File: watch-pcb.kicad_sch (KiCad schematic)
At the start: 12 parts, among them J1 DAUGHTER

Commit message: quicksaving pcb bc im gonna redo it
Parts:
- removed R1, R2, R8: 10k, Resistor_SMD:R_0402_1005Metric, symbol Device:R
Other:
- removed sheet STM MCU
- added sheet ESP MCU (esp_mcu.kicad_sch)
- sheet IO ports: added ALT_SCL, ALT_SDA, HBT_SCL, HBT_SDA, IMU_SCL, IMU_SDA, MAG_SCL, MAG_SDA, MTR_SCL, MTR_SDA, SD_CLK, SD_CMD, SD_D0, SD_D1, SD_D2, SD_D3, TP_SCL, TP_SDA; removed SCL1, SCL2, SCL3, SDA1, SDA2, SDA3, TP_COM_EN
- sheet USB and Power ports: added USB_DM, USB_DP; removed BOOT, MCU_RST, UART_RX, UART_TX
- moved on the sheet: D1, D15, J1, R3, R4, R5, R55, R6, R7

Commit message: no more daughter probably
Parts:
- renumbered D15 to D1, D1 to D2, R4 to R1, R5 to R2, R6 to R3, R7 to R4, R55 to R5, R3 to R6
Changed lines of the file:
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@@
 		(on_board yes)
 		(dnp no)
-		(property "Reference" "#PWR06"
+		(property "Reference" "#PWR01"
 			(at 224.79 27.94 0)
 			(effects
@@
 			(project "watch-pcb"
 				(path "/b7b86b03-b0df-4b4e-be1d-606605306dad"
-					(reference "#PWR06")
+					(reference "#PWR01")
 					(unit 1)
 				)
@@
 		(on_board yes)
 		(dnp no)
-		(property "Reference" "R6"
+		(property "Reference" "R3"
 			(at 228.6 29.21 0)
 			(effects
@@
 			(project "watch-pcb"
 				(path "/b7b86b03-b0df-4b4e-be1d-606605306dad"
-					(reference "R6")
+					(reference "R3")
 					(unit 1)
 				)
@@
 		(on_board yes)
 		(dnp no)
-		(property "Reference" "#PWR05"
+		(property "Reference" "#PWR03"
 			(at 69.85 118.11 0)
 			(effects
@@
 			(project "watch-pcb"
 				(path "/b7b86b03-b0df-4b4e-be1d-606605306dad"
-					(reference "#PWR05")
+					(reference "#PWR03")
 					(unit 1)
 				)
@@
 		(on_board yes)
 		(dnp no)
-		(property "Reference" "R3"
+		(property "Reference" "R6"
 			(at 69.85 162.56 90)
 			(effects
@@
 			(project "watch-pcb"
 				(path "/b7b86b03-b0df-4b4e-be1d-606605306dad"
-					(reference "R3")
+					(reference "R6")
 					(unit 1)
 				)
@@
 		(on_board yes)
 		(dnp no)
-		(property "Reference" "#PWR03"
+		(property "Reference" "#PWR02"
 			(at 63.5 118.11 0)
 			(effects
@@
 			(project "watch-pcb"
 				(path "/b7b86b03-b0df-4b4e-be1d-606605306dad"
-					(reference "#PWR03")
+					(reference "#PWR02")
 					(unit 1)
 				)
@@
 		(on_board yes)
 		(dnp no)
-		(property "Reference" "D15"
+		(property "Reference" "D1"
 			(at 60.96 154.94 0)
 			(effects
@@
 			(project "watch-pcb"
 				(path "/b7b86b03-b0df-4b4e-be1d-606605306dad"
-					(reference "D15")
+					(reference "D1")
 					(unit 1)
 				)
@@
 		(dnp no)
 		(fields_autoplaced yes)
-		(property "Reference" "#PWR021"
+		(property "Reference" "#PWR05"
 			(at 50.8 160.02 0)
 			(effects
@@
 			(project "watch-pcb"
 				(path "/b7b86b03-b0df-4b4e-be1d-606605306dad"
-					(reference "#PWR021")
+					(reference "#PWR05")
 					(unit 1)
 				)
@@
 		(on_board yes)
 		(dnp no)
-		(property "Reference" "R7"
+		(property "Reference" "R4"
 			(at 237.49 29.21 0)
 			(effects
@@
 			(project "watch-pcb"
 				(path "/b7b86b03-b0df-4b4e-be1d-606605306dad"
-					(reference "R7")
+					(reference "R4")
 					(unit 1)
 				)
@@
 		(dnp no)
 		(fields_autoplaced yes)
-		(property "Reference" "#PWR01"
+		(property "Reference" "#PWR06"
 			(at 50.8 165.1 0)
 			(effects
@@
 			(project "watch-pcb"
 				(path "/b7b86b03-b0df-4b4e-be1d-606605306dad"
-					(reference "#PWR01")
+					(reference "#PWR06")
 					(unit 1)
 				)
@@
 		(on_board yes)
 		(dnp no)
-		(property "Reference" "R4"
+		(property "Reference" "R1"
 			(at 215.9 29.21 0)
 			(effects
@@
 			(project "watch-pcb"
 				(path "/b7b86b03-b0df-4b4e-be1d-606605306dad"
-					(reference "R4")
+					(reference "R1")
 					(unit 1)
 				)
@@
 		(on_board yes)
 		(dnp no)
-		(property "Reference" "R55"
+		(property "Reference" "R5"
 			(at 69.85 157.48 90)
 			(effects
@@
 			(project "watch-pcb"
 				(path "/b7b86b03-b0df-4b4e-be1d-606605306dad"
-					(reference "R55")
+					(reference "R5")
 					(unit 1)
 				)
@@
 		(on_board yes)
 		(dnp no)
-		(property "Reference" "D1"
+		(property "Reference" "D2"
 			(at 62.23 167.64 0)
 			(effects
@@
 			(project "watch-pcb"
 				(path "/b7b86b03-b0df-4b4e-be1d-606605306dad"
-					(reference "D1")
+					(reference "D2")
 					(unit 1)
 				)
@@
 		(on_board yes)
 		(dnp no)
-		(property "Reference" "R5"
+		(property "Reference" "R2"
 			(at 224.79 29.21 0)
 			(effects
@@
 			(project "watch-pcb"
 				(path "/b7b86b03-b0df-4b4e-be1d-606605306dad"
-					(reference "R5")
-					(unit 1)
-				)
+					(reference "R2")
+					(unit 1)
+				)

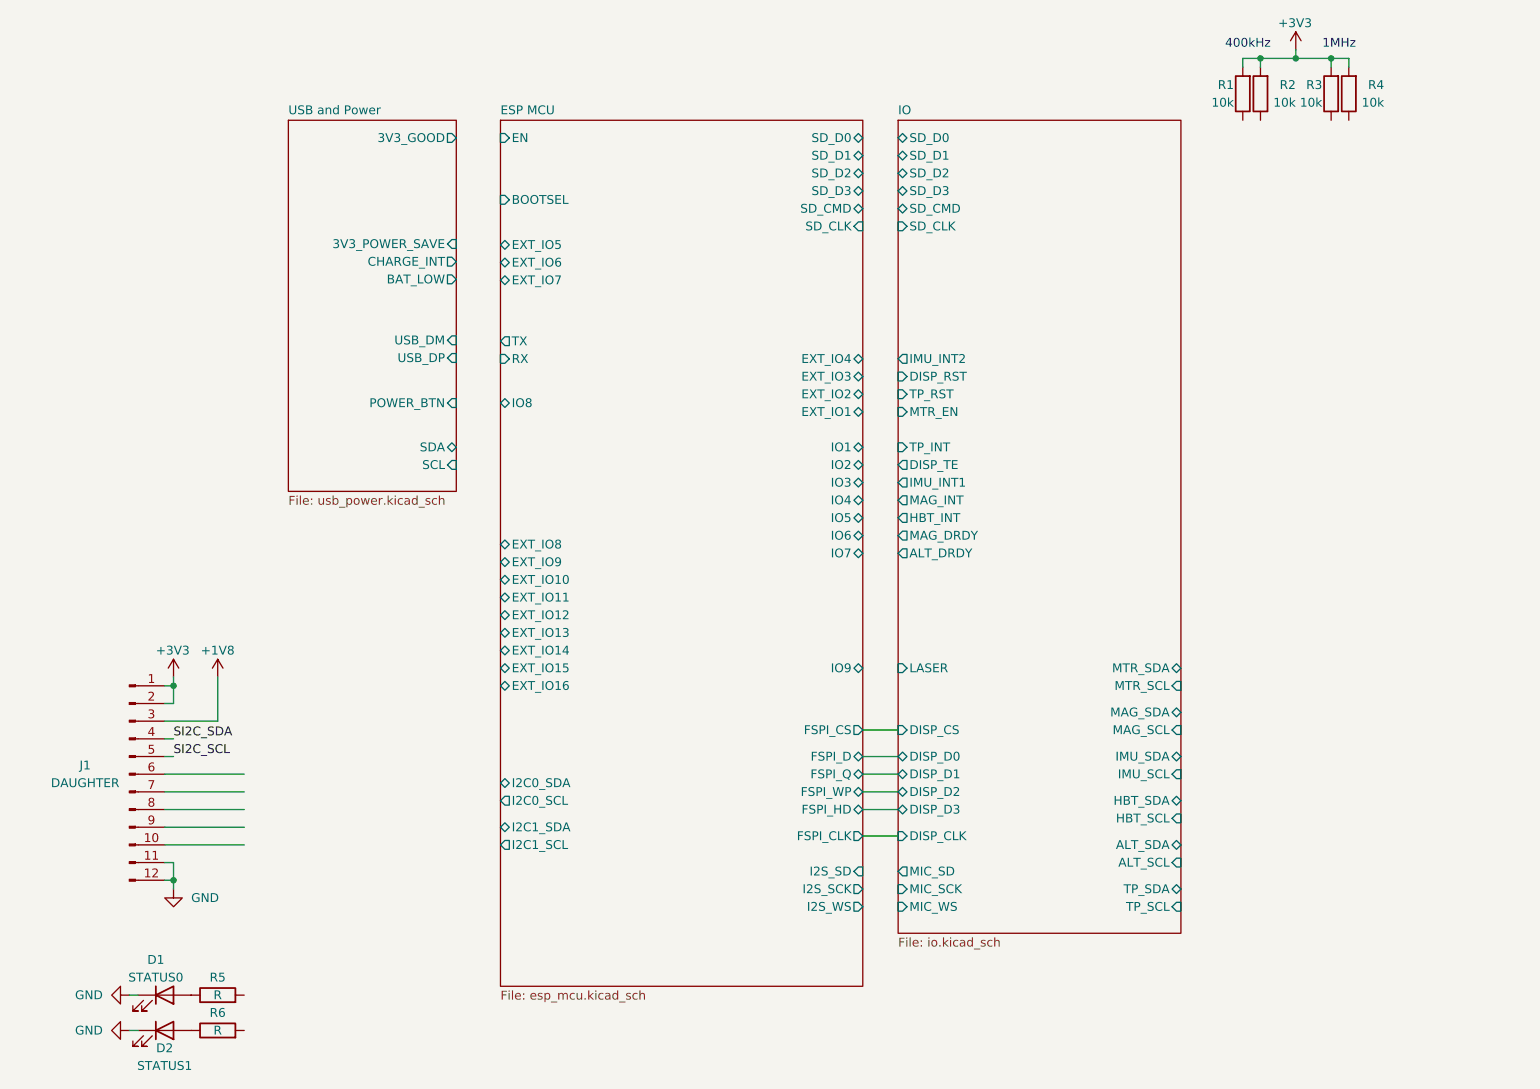
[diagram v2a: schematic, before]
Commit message: basically done with board layout, gonna try to do a smaller one (47->42mm diameter)
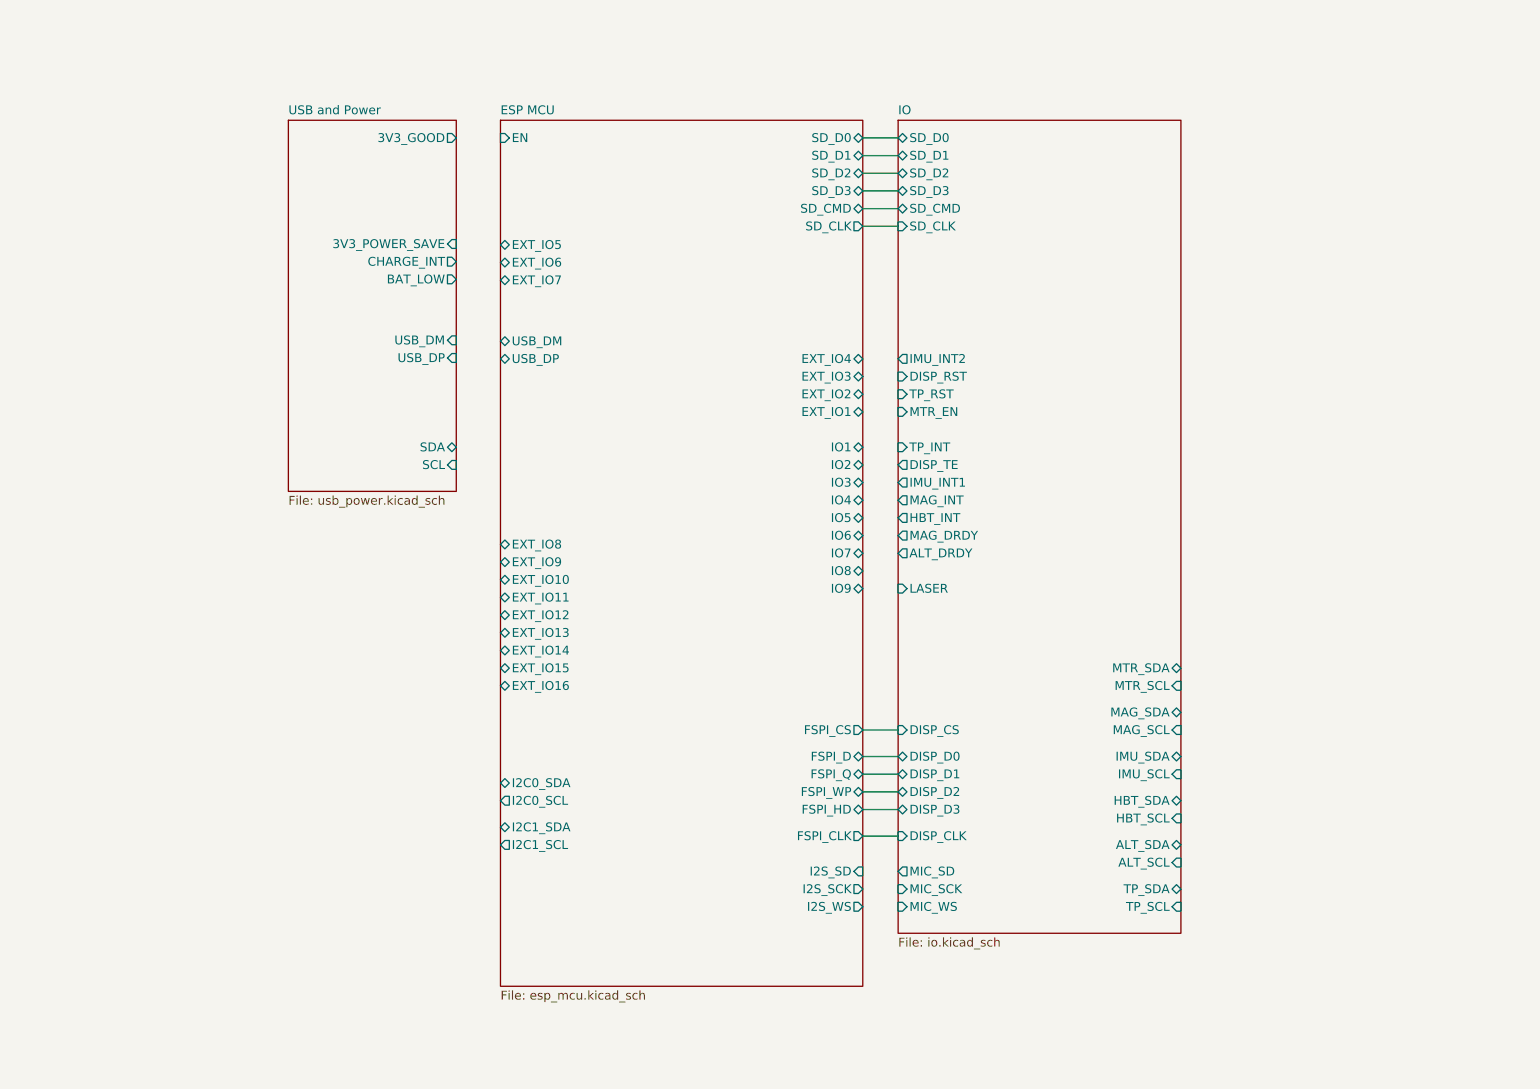
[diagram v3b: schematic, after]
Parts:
- removed D1: STATUS0, LED_SMD:LED_0402_1005Metric, symbol Device:LED
- removed D2: STATUS1, LED_SMD:LED_0402_1005Metric, symbol Device:LED
- removed J1: DAUGHTER, Connector_FFC-FPC:TE_1-1734839-2_1x12-1MP_P0.5mm_Horizontal, symbol Connector:Conn_01x12_Pin
- removed R1, R2, R3, R4: 10k, Resistor_SMD:R_0402_1005Metric, symbol Device:R
- removed R5, R6: R, Resistor_SMD:R_0402_1005Metric, symbol Device:R
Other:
- sheet ESP MCU ports: added USB_DM, USB_DP; removed BOOTSEL, RX, TX
- sheet USB and Power ports: added none; removed POWER_BTN
- note removed: "1MHz"
- note removed: "400kHz"

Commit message: layout done probably
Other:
- sheet ESP MCU ports: added none; removed IO9
- sheet IO ports: added ALS_INT, ALS_SCL, ALS_SDA, BTN_1, BTN_2, BTN_3, LIGHT; removed none

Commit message: finally routed the memory :D
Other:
- sheet ESP MCU ports: added IO9, USB_D+, USB_D-; removed USB_DM, USB_DP
- sheet USB and Power ports: added QON, USB_D+, USB_D-; removed USB_DM, USB_DP
- note added: "100 mA max 1V8 1 A max 3V3 1 A max system current"
- note added: "400 mA max 3V3 440 mA max total"
- note added: "70 mA max 1V8 500 mA max 3V3 570 mA max total"
- note added: "Good"
